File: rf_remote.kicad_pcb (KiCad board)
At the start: 2 copper layers, 57.3 x 26.5 mm, 17 parts, among them P1 CONN_01X04, P2 CONN_01X01, U1 SAMD21E18, U2 RFM69CW-915MHZ

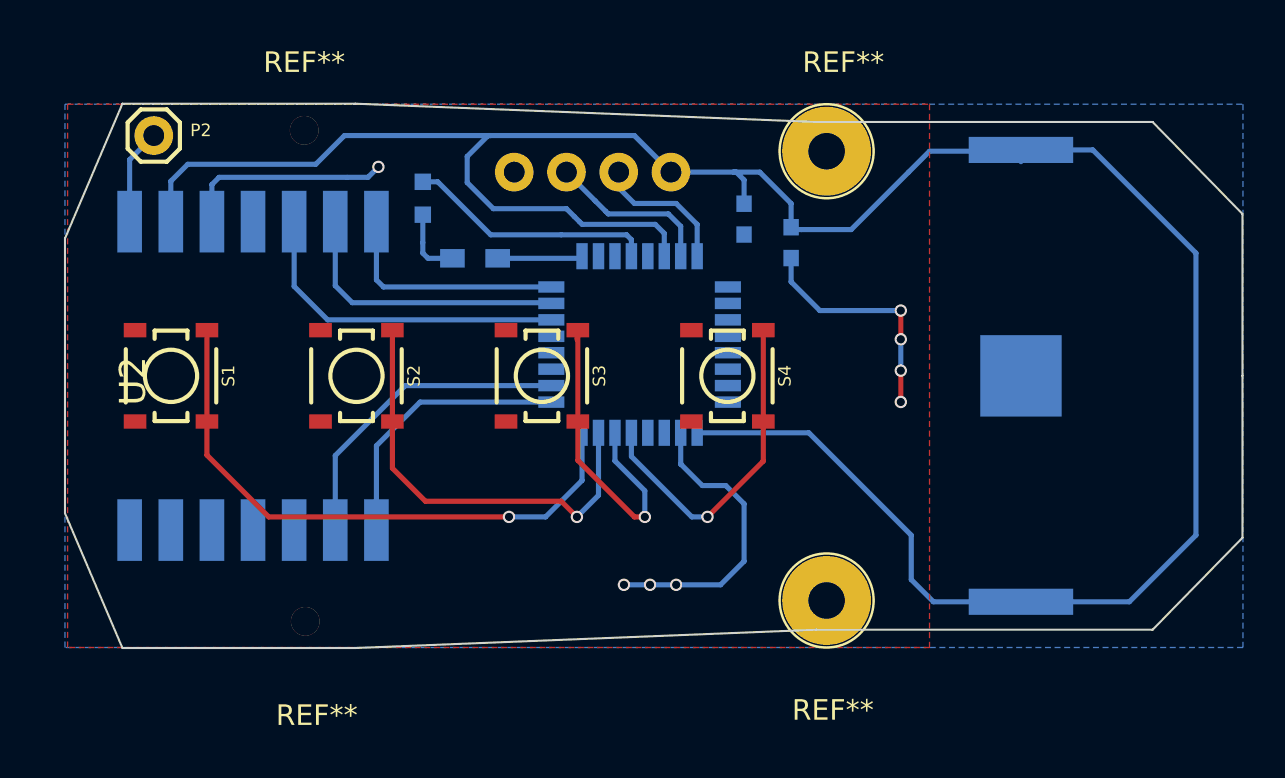
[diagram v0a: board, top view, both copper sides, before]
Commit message: Added USB port and updated switch footprint
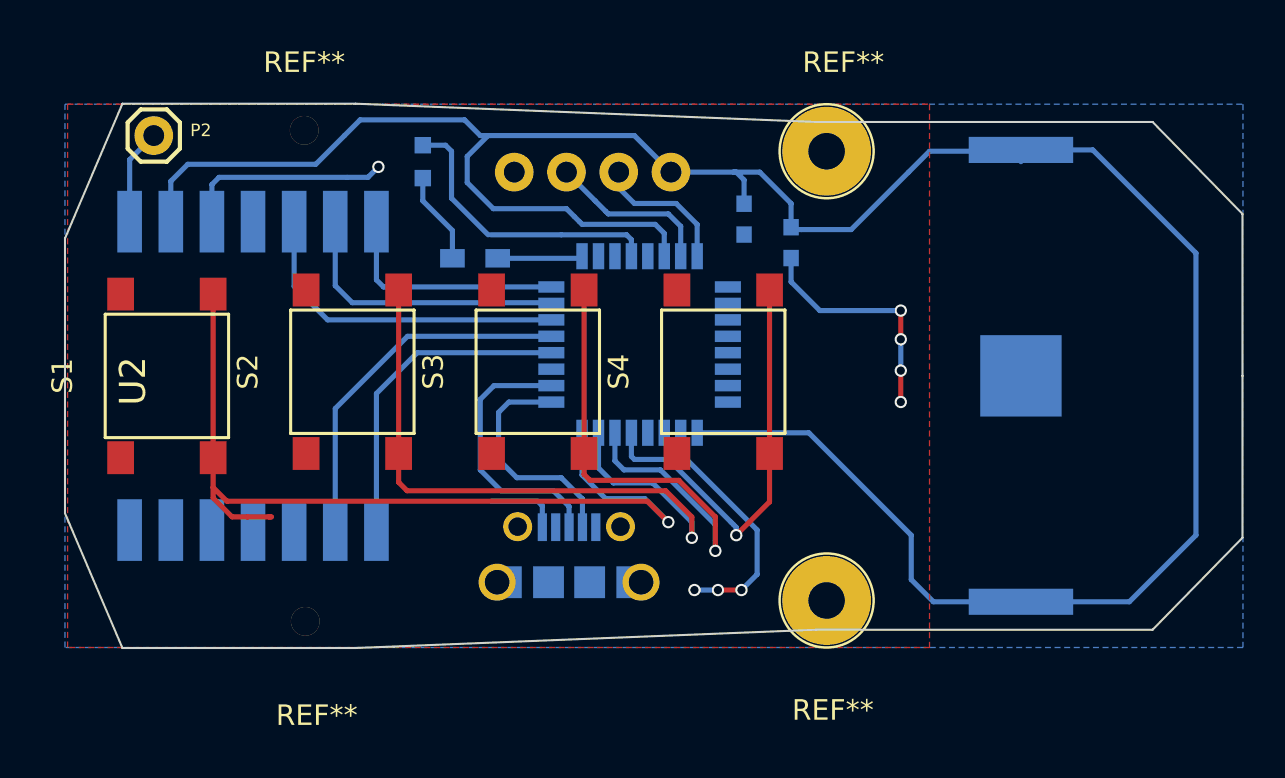
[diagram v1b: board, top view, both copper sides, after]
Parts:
- added J1: 10118194-0001LF, 10118194-0001LF:FRAMATOME_10118194-0001LF, B.Cu at (100.7, 86.2)
- S1, S2, S3, S4: value MOMENTARY-SWITCH-SPST-SMD-4.5MM -> MOMENTARY-SWITCH-6x6x4.5mm; footprint SF_Switches:TACTILE_SWITCH_SMD_4.5MM -> homebrew_button:6x6x4.3mm button
- moved D1 1.78 mm to (93.6, 65.8)
- moved S4 0.28 mm to (108.2, 76.0), turned to 90 degrees
- moved S2 0.28 mm to (90.2, 76.0), turned to 90 degrees
- moved S3 0.28 mm to (99.2, 76.0), turned to 90 degrees
- moved S1 0.20 mm to (81.2, 76.2), turned to 90 degrees
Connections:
- S1 pad 1: SW1 -> GND
- S1 pad 3: GND -> SW1
- S2 pad 1: SW2 -> GND
- S2 pad 3: GND -> SW2
- S3 pad 1: SW3 -> GND
- S3 pad 3: GND -> SW3
- S4 pad 1: SW4 -> GND
- S4 pad 3: GND -> SW4
- U1 pad 17: RADIO_MISO -> USB_D-
- U1 pad 18: RADIO_DIO0 -> USB_D+
- U1 pad 20: Net-(U1-Pad20) -> RADIO_MISO
- U1 pad 21: Net-(U1-Pad21) -> RADIO_DIO0
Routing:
- net SW1: track 28.7 -> 43.3 mm
- net USB_D+: track 0.00 -> 13.2 mm
- net SW2: track 21.3 -> 33.4 mm
- net USB_D-: track 0.00 -> 11.3 mm
- net SW3: track 15.9 -> 26.7 mm
- net SW4: track 16.3 -> 20.6 mm
- net GND: track 48.5 -> 51.3 mm
- net RADIO_MISO: track 13.5 -> 16.0 mm
- net RADIO_DIO0: track 15.5 -> 17.9 mm
- net Net-(D1-Pad2): track 3.41 -> 4.50 mm
- net +3V3: track 119.9 -> 120.4 mm

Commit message: Changed microcontroller wiring to original pin layout. Now with added vias!
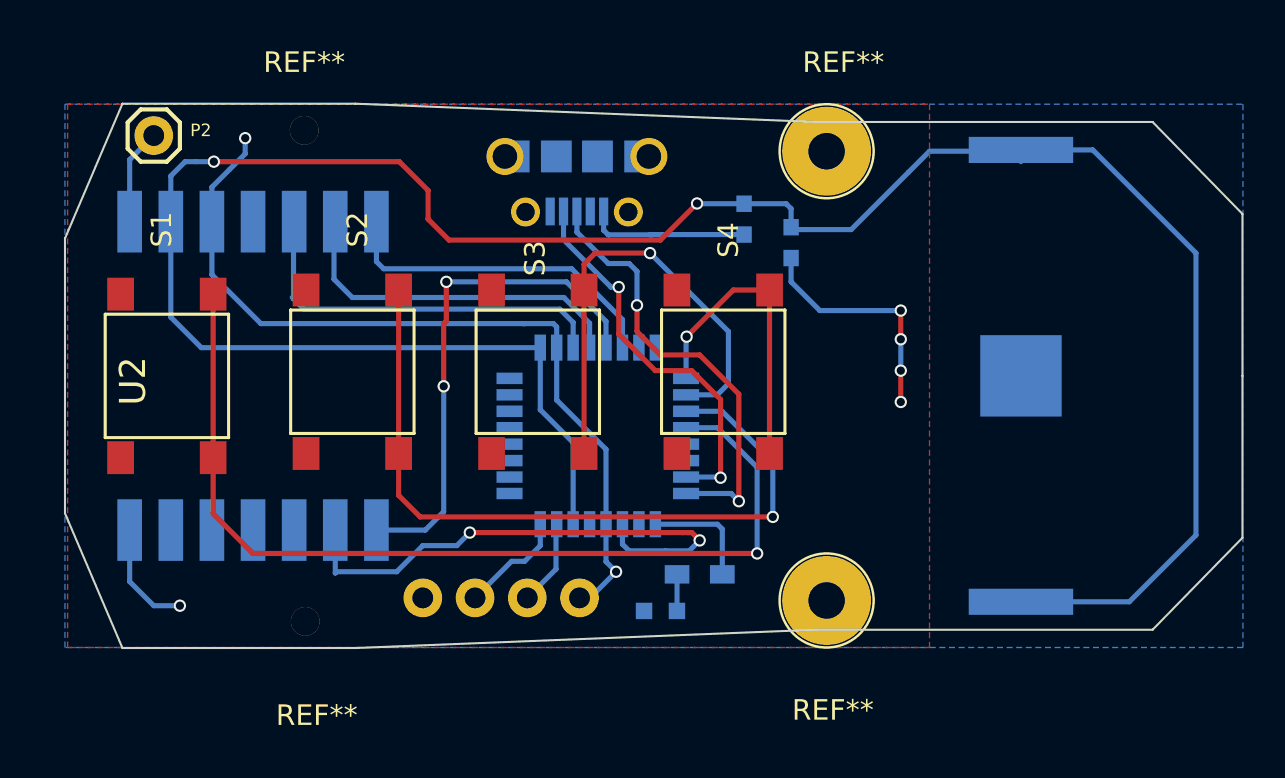
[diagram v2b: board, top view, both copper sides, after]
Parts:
- moved D1 24.7 mm to (105.2, 87.6), turned to 0 degrees
- moved P1 24.0 mm to (93.6, 87.0), turned to 0 degrees
- moved J1 20.7 mm to (101.1, 65.5), turned to 0 degrees
- moved R1 18.9 mm to (107.1, 85.9)
- moved U1 4.89 mm to (102.1, 79.1), turned to 0 degrees
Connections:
- P1 pad 1: +3V3 -> Net-(P1-Pad1)
- U1 pad 11: Net-(U1-Pad11) -> RADIO_MOSI
- U1 pad 12: Net-(U1-Pad12) -> RADIO_SCK
- U1 pad 13: SW4 -> RADIO_MISO
- U1 pad 14: SW3 -> RADIO_NSS
- U1 pad 15: SW2 -> Net-(U1-Pad15)
- U1 pad 16: SW1 -> Net-(U1-Pad16)
- U1 pad 17: USB_D- -> SW4
- U1 pad 18: USB_D+ -> SW3
- U1 pad 19: Net-(U1-Pad19) -> SW2
- U1 pad 20: RADIO_MISO -> SW1
- U1 pad 21: RADIO_DIO0 -> Net-(U1-Pad21)
- U1 pad 22: RADIO_MOSI -> Net-(U1-Pad22)
- U1 pad 23: RADIO_SCK -> USB_D-
- U1 pad 24: RADIO_NSS -> USB_D+
- U1 pad 27: Net-(U1-Pad27) -> RADIO_DIO0
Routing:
- net GND: track 51.3 -> 65.7 mm, vias 8 -> 7
- net RADIO_MISO: track 16.0 -> 24.7 mm, vias 0 -> 2
- net USB_D+: track 13.2 -> 21.8 mm, vias 0 -> 2
- net RADIO_DIO0: track 17.9 -> 26.1 mm, vias 0 -> 2
- net USB_D-: track 11.3 -> 19.1 mm, vias 0 -> 2
- net SW4: track 20.6 -> 15.0 mm
- net RADIO_NSS: track 11.5 -> 16.4 mm
- net ARM_SWCLK: track 8.10 -> 4.17 mm
- net SW3: track 26.7 -> 22.8 mm
- net +3V3: track 120.4 -> 116.8 mm, vias 0 -> 2
- net RADIO_SCK: track 14.0 -> 17.3 mm
- net SW2: track 33.4 -> 36.5 mm
- net SW1: track 43.3 -> 46.4 mm
- net RADIO_MOSI: track 16.3 -> 19.2 mm
- net Net-(D1-Pad2): track 4.50 -> 1.78 mm
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
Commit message: Hardware revision v1.1: - Add USB port - Don't connect VCC on SWD to anything
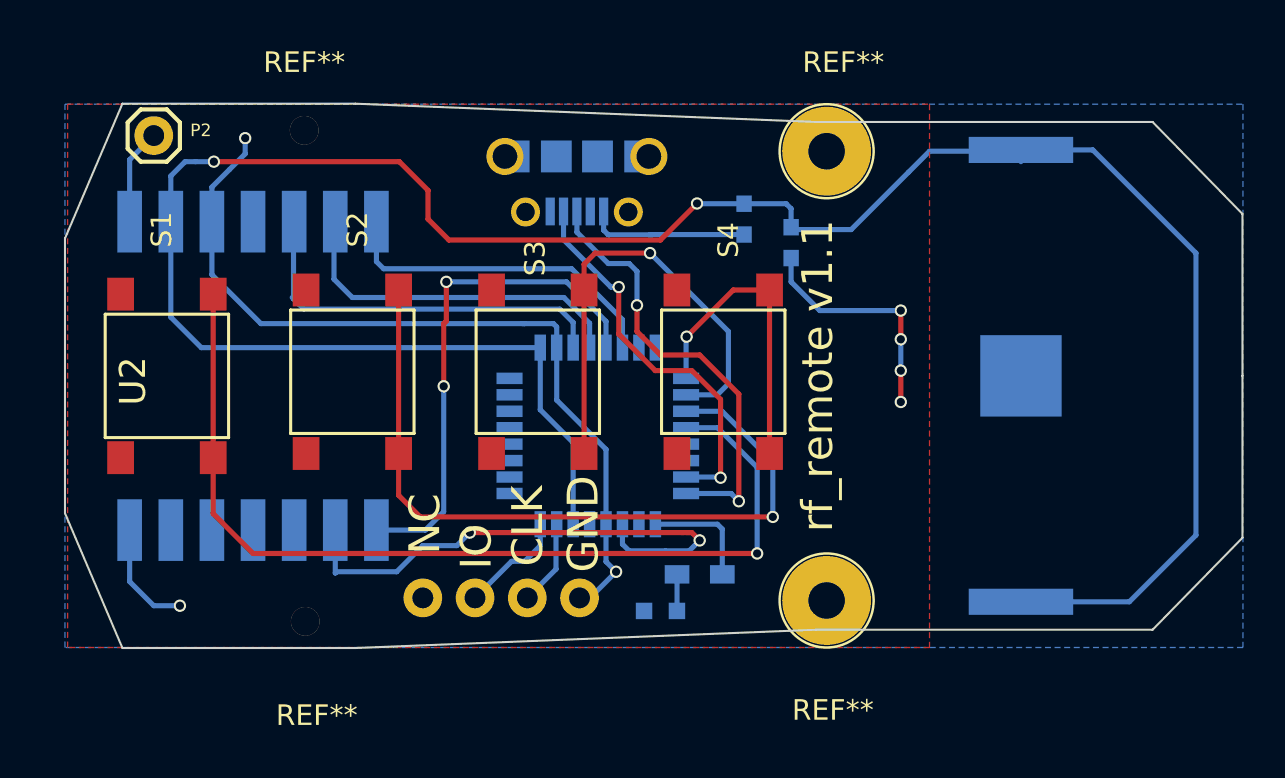
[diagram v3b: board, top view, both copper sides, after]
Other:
- board text added: "CLK"
- board text added: "G"
- board text added: "GND"
- board text added: "IO"
- board text added: "NC"
- board text added: "rf_remote v1.1"
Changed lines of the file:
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@@
-(kicad_pcb (version 4) (host pcbnew 4.0.7-e2-6376~58~ubuntu16.04.1)
+(kicad_pcb (version 4) (host pcbnew 4.0.7-e2-6376~61~ubuntu18.04.1)
   (general
     (links 43)
@@
     (area 76.149999 62.916599 133.501601 89.483401)
     (thickness 1.6)
-    (drawings 14)
+    (drawings 23)
     (tracks 196)
     (zones 0)
@@
     (visible_elements FFFFFF7F)
     (pcbplotparams
-      (layerselection 0x00030_80000001)
+      (layerselection 0x3f0ff_80000001)
       (usegerberextensions false)
       (excludeedgelayer true)
@@
       (psnegative false)
       (psa4output false)
-      (plotreference true)
-      (plotvalue true)
+      (plotreference false)
+      (plotvalue false)
       (plotinvisibletext false)
       (padsonsilk false)
@@
       (outputformat 1)
       (mirror false)
-      (drillshape 1)
+      (drillshape 0)
       (scaleselection 1)
-      (outputdirectory ""))
+      (outputdirectory gerber))
   )
   (net 0 "")
@@
       (net 1 GND))
   )
+  (gr_text "rf_remote v1.1" (at 112.8 76.2 90) (layer F.SilkS)
+    (effects (font (size 1.5 1.5) (thickness 0.3)))
+  )
+  (gr_text NC (at 93.7 83.4 90) (layer F.SilkS)
+    (effects (font (size 1.5 1.5) (thickness 0.3)))
+  )
+  (gr_text IO (at 96.2 84.5 90) (layer F.SilkS)
+    (effects (font (size 1.5 1.5) (thickness 0.3)))
+  )
+  (gr_text CLK (at 98.7 83.5 90) (layer F.SilkS)
+    (effects (font (size 1.5 1.5) (thickness 0.3)))
+  )
+  (gr_text GND (at 101.4 83.4 90) (layer F.SilkS)
+    (effects (font (size 1.5 1.5) (thickness 0.3)))
+  )
+  (gr_text NC (at 93.5 84.8) (layer B.SilkS)
+    (effects (font (size 0.8 0.8) (thickness 0.1)) (justify mirror))
+  )
+  (gr_text IO (at 96.2 84.9) (layer B.SilkS)
+    (effects (font (size 0.8 0.8) (thickness 0.1)) (justify mirror))
+  )
+  (gr_text CLK (at 98.6 84.9) (layer B.SilkS)
+    (effects (font (size 0.8 0.8) (thickness 0.1)) (justify mirror))
+  )
+  (gr_text G (at 101.2 85) (layer B.SilkS)
+    (effects (font (size 0.8 0.8) (thickness 0.1)) (justify mirror))
+  )
   (gr_line (start 76.2 76.2) (end 76.2 69.5198) (angle 90) (layer Edge.Cuts) (width 0.1))
   (gr_line (start 76.2 69.5198) (end 78.994 62.9666) (angle 90) (layer Edge.Cuts) (width 0.1))
@@
   (gr_line (start 76.2 82.8802) (end 78.994 89.4334) (angle 90) (layer Edge.Cuts) (width 0.1))
   (gr_line (start 76.2 76.2) (end 76.2 82.8802) (angle 90) (layer Edge.Cuts) (width 0.1))
-  (segment (start 83.34502 68.70192) (end 83.34502 71.28002) (width 0.25) (layer B.Cu) (net 1) (status 400000))
+  (segment (start 83.34502 68.70192) (end 83.34502 71.28002) (width 0.25) (layer B.Cu) (net 1))
   (segment (start 85.725 73.66) (end 98.552 73.66) (width 0.25) (layer B.Cu) (net 1))
   (segment (start 83.34502 71.28002) (end 85.725 73.66) (width 0.25) (layer B.Cu) (net 1))
-  (segment (start 109.22 69.33) (end 104.66 69.33) (width 0.25) (layer B.Cu) (net 1) (status 400000))
+  (segment (start 109.22 69.33) (end 104.66 69.33) (width 0.25) (layer B.Cu) (net 1))
   (segment (start 104.66 69.33) (end 104.648 69.342) (width 0.25) (layer B.Cu) (net 1))
-  (segment (start 102.392 68.207) (end 102.392 69.118) (width 0.25) (layer B.Cu) (net 1) (status 400000))
+  (segment (start 102.392 68.207) (end 102.392 69.118) (width 0.25) (layer B.Cu) (net 1))
   (segment (start 102.616 69.342) (end 104.648 69.342) (width 0.25) (layer B.Cu) (net 1))
   (segment (start 104.648 69.342) (end 104.775 69.342) (width 0.25) (layer B.Cu) (net 1))
   (segment (start 102.392 69.118) (end 102.616 69.342) (width 0.25) (layer B.Cu) (net 1))
-  (segment (start 102.50678 83.4136) (end 102.50678 85.23478) (width 0.25) (layer B.Cu) (net 1) (status 400000))
+  (segment (start 102.50678 83.4136) (end 102.50678 85.23478) (width 0.25) (layer B.Cu) (net 1))
   (via (at 102.997 85.725) (size 0.6) (drill 0.4) (layers F.Cu B.Cu) (net 1))
-  (segment (start 102.997 85.725) (end 101.727 86.995) (width 0.25) (layer B.Cu) (net 1) (status 800000))
+  (segment (start 102.997 85.725) (end 101.727 86.995) (width 0.25) (layer B.Cu) (net 1))
   (segment (start 102.50678 85.23478) (end 102.997 85.725) (width 0.25) (layer B.Cu) (net 1))
-  (segment (start 101.219 86.995) (end 101.727 86.995) (width 0.25) (layer B.Cu) (net 1) (status C00000))
-  (segment (start 100.10902 74.8284) (end 100.10902 77.37602) (width 0.25) (layer B.Cu) (net 1) (status 400000))
-  (segment (start 102.50678 79.77378) (end 102.50678 83.4136) (width 0.25) (layer B.Cu) (net 1) (status 800000))
+  (segment (start 101.219 86.995) (end 101.727 86.995) (width 0.25) (layer B.Cu) (net 1))
+  (segment (start 100.10902 74.8284) (end 100.10902 77.37602) (width 0.25) (layer B.Cu) (net 1))
+  (segment (start 102.50678 79.77378) (end 102.50678 83.4136) (width 0.25) (layer B.Cu) (net 1))
   (segment (start 100.10902 77.37602) (end 102.50678 79.77378) (width 0.25) (layer B.Cu) (net 1))
-  (segment (start 79.34452 83.69808) (end 79.34452 86.20252) (width 0.25) (layer B.Cu) (net 1) (status 400000))
+  (segment (start 79.34452 83.69808) (end 79.34452 86.20252) (width 0.25) (layer B.Cu) (net 1))
   (via (at 81.788 87.376) (size 0.6) (drill 0.4) (layers F.Cu B.Cu) (net 1))
   (segment (start 80.518 87.376) (end 81.788 87.376) (width 0.25) (layer B.Cu) (net 1))
   (segment (start 79.34452 86.20252) (end 80.518 87.376) (width 0.25) (layer B.Cu) (net 1))
-  (segment (start 83.34502 68.70192) (end 83.34502 67.02298) (width 0.25) (layer B.Cu) (net 1) (status 400000))
+  (segment (start 83.34502 68.70192) (end 83.34502 67.02298) (width 0.25) (layer B.Cu) (net 1))
   (via (at 84.963 64.643) (size 0.6) (drill 0.4) (layers F.Cu B.Cu) (net 1))
   (segment (start 84.963 65.405) (end 84.963 64.643) (width 0.25) (layer B.Cu) (net 1))
   (segment (start 84.201 66.167) (end 84.963 65.405) (width 0.25) (layer B.Cu) (net 1))
   (segment (start 83.34502 67.02298) (end 84.201 66.167) (width 0.25) (layer B.Cu) (net 1))
-  (segment (start 100.10902 74.8284) (end 100.10902 73.82002) (width 0.25) (layer B.Cu) (net 1) (status 400000))
+  (segment (start 100.10902 74.8284) (end 100.10902 73.82002) (width 0.25) (layer B.Cu) (net 1))
   (segment (start 100.10902 73.82002) (end 99.949 73.66) (width 0.25) (layer B.Cu) (net 1))
   (segment (start 99.949 73.66) (end 98.552 73.66) (width 0.25) (layer B.Cu) (net 1))
@@
   (segment (start 111.506 71.628) (end 112.903 73.025) (width 0.25) (layer B.Cu) (net 1))
   (segment (start 100.711 86.868) (end 100.711 86.741) (width 0.25) (layer B.Cu) (net 1))
-  (segment (start 109.22 67.83) (end 106.946 67.83) (width 0.25) (layer B.Cu) (net 2) (status 400000))
-  (segment (start 81.34604 66.48196) (end 81.34604 68.70192) (width 0.25) (layer B.Cu) (net 2) (status 800000))
+  (segment (start 109.22 67.83) (end 106.946 67.83) (width 0.25) (layer B.Cu) (net 2))
+  (segment (start 81.34604 66.48196) (end 81.34604 68.70192) (width 0.25) (layer B.Cu) (net 2))
   (segment (start 82.042 65.786) (end 81.34604 66.48196) (width 0.25) (layer B.Cu) (net 2))
   (segment (start 82.55 65.786) (end 82.042 65.786) (width 0.25) (layer B.Cu) (net 2))
@@
   (via (at 106.934 67.818) (size 0.6) (drill 0.4) (layers F.Cu B.Cu) (net 2))
   (segment (start 106.946 67.83) (end 106.934 67.818) (width 0.25) (layer B.Cu) (net 2))
-  (segment (start 99.30892 74.8284) (end 82.8294 74.8284) (width 0.25) (layer B.Cu) (net 2) (status 400000))
+  (segment (start 99.30892 74.8284) (end 82.8294 74.8284) (width 0.25) (layer B.Cu) (net 2))
   (segment (start 82.8294 74.8284) (end 81.34604 73.34504) (width 0.25) (layer B.Cu) (net 2))
-  (segment (start 81.34604 73.34504) (end 81.34604 68.70192) (width 0.25) (layer B.Cu) (net 2) (status 800000))
+  (segment (start 81.34604 73.34504) (end 81.34604 68.70192) (width 0.25) (layer B.Cu) (net 2))
   (segment (start 100.90912 83.4136) (end 100.90912 79.44612) (width 0.25) (layer B.Cu) (net 2))
   (segment (start 99.30892 77.84592) (end 99.30892 74.8284) (width 0.25) (layer B.Cu) (net 2))
